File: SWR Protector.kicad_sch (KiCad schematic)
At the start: 29 parts, among them J1 Barrel_Jack, J2 Barrel_Jack, J3 transceiver, J4 antenna, K2 ATX209, Q1 2N3904, T1 1:12, T2 1:12, U1 LM78L05_TO92, U2 LM358

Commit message: updated BNC to something reasonable, w/ Ron\'s help
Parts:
- J3, J4: footprint Connector_Coaxial:BNC_TEConnectivity_1478035_Horizontal -> Connector_Coaxial:BNC_Amphenol_B6252HB-NPP3G-50_Horizontal
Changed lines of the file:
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@@
   (title_block
     (title "SWR Protector WA7GIL")
-    (date "2023-05-09")
-    (rev "0.6")
+    (date "2023-05-10")
+    (rev "0.7")
   )
   (junction (at 181.61 138.43) (diameter 0) (color 0 0 0 0)
@@
       (effects (font (size 1.27 1.27)) (justify left))
     )
-    (property "Footprint" "Connector_Coaxial:BNC_TEConnectivity_1478035_Horizontal" (at 134.62 35.56 0)
+    (property "Footprint" "Connector_Coaxial:BNC_Amphenol_B6252HB-NPP3G-50_Horizontal" (at 134.62 35.56 0)
       (effects (font (size 1.27 1.27)) hide)
     )
@@
       (effects (font (size 1.27 1.27)) (justify left))
     )
-    (property "Footprint" "Connector_Coaxial:BNC_TEConnectivity_1478035_Horizontal" (at 48.26 35.56 0)
-      (effects (font (size 1.27 1.27)) hide)
-    )
+    (property "Footprint" "Connector_Coaxial:BNC_Amphenol_B6252HB-NPP3G-50_Horizontal" (at 48.26 35.56 0)
+      (effects (font (size 1.27 1.27)) hide)
+    )

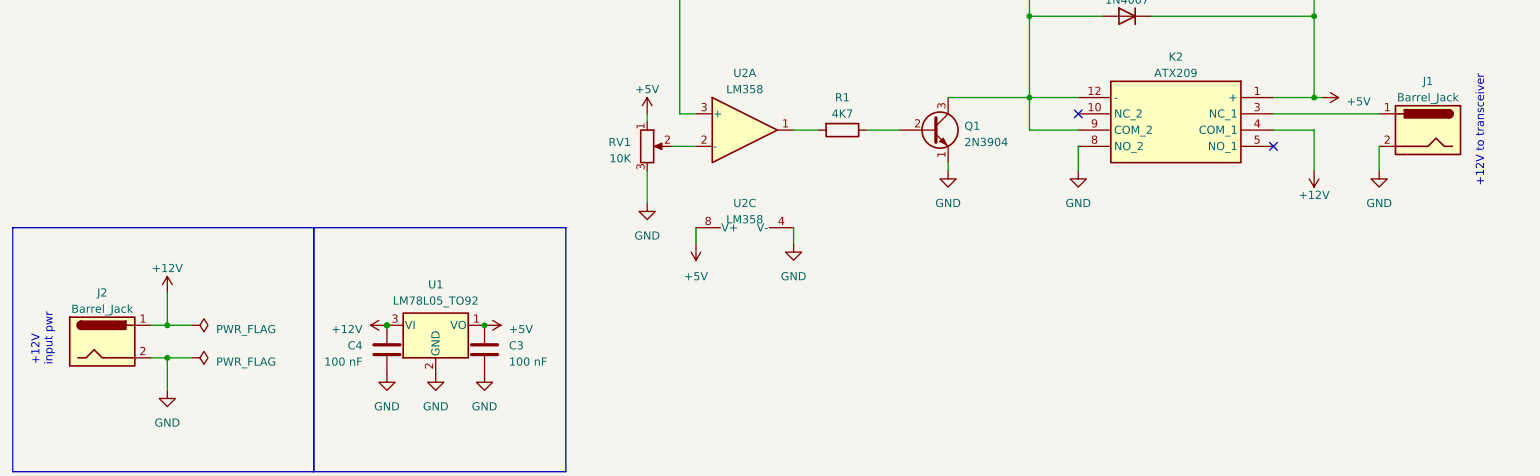
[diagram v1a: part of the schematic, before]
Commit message: changed footprint for BNC, barrel connectors to make them normal
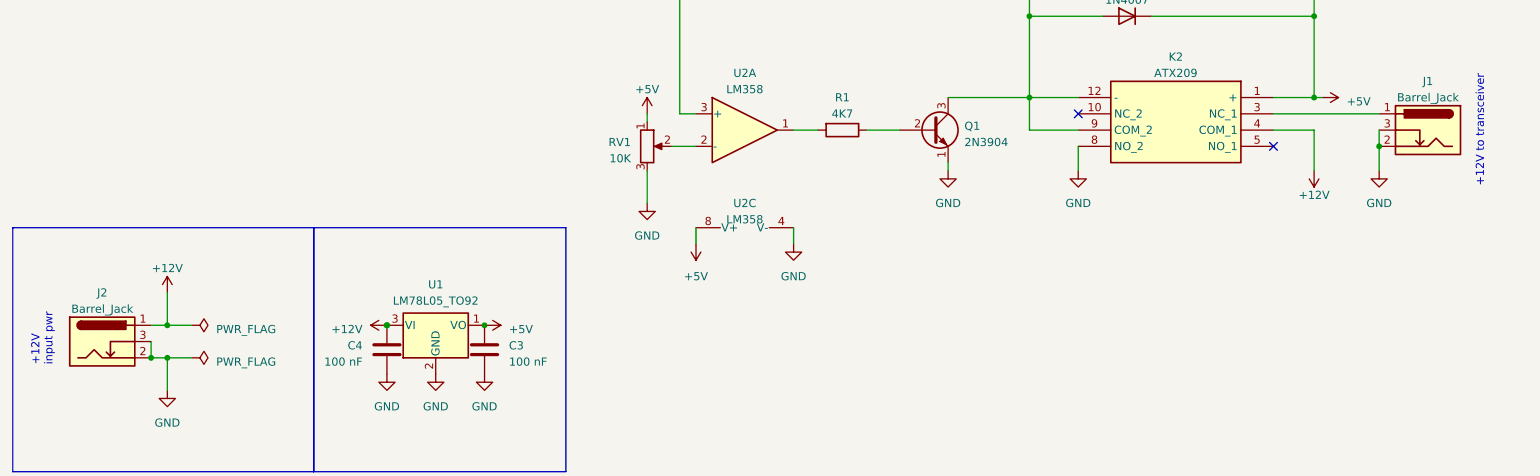
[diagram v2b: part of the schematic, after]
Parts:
- removed J1, J2: Barrel_Jack, Connector_BarrelJack:BarrelJack_CUI_PJ-063AH_Horizontal, symbol Connector:Barrel_Jack
- added J1, J2: Barrel_Jack, Connector_BarrelJack:BarrelJack_Horizontal, symbol Connector:Barrel_Jack_Switch
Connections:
- net +12V: now also J2.1
- net GND: now also J1.2, J1.3, J2.2, J2.3
- net at K2.3 (NC_1): now also J1.1
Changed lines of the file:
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@@
     (rev "0.7")
   )
+  (junction (at 44.45 179.07) (diameter 0) (color 0 0 0 0)
+  )
   (junction (at 181.61 138.43) (diameter 0) (color 0 0 0 0)
   )
@@
   )
   (junction (at 134.62 80.01) (diameter 0) (color 0 0 0 0)
+  )
+  (junction (at 236.22 146.05) (diameter 0) (color 0 0 0 0)
   )
   (junction (at 134.62 60.96) (diameter 0) (color 0 0 0 0)
@@
     (stroke (width 0) (type default))
   )
+  (wire (pts (xy 44.45 176.53) (xy 44.45 179.07))
+    (stroke (width 0) (type default))
+  )
   (wire (pts (xy 181.61 114.3) (xy 181.61 125.73))
     (stroke (width 0) (type default))
@@
   )
   (wire (pts (xy 49.53 80.01) (xy 50.8 80.01))
+    (stroke (width 0) (type default))
+  )
+  (wire (pts (xy 236.22 143.51) (xy 236.22 146.05))
     (stroke (width 0) (type default))
   )
@@
         (path "/46027dd5-036f-43c6-98e1-c4cfe473ecd7"
           (reference "D1") (unit 1)
-        )
-      )
-    )
-  )
-  (symbol (lib_id "Connector:Barrel_Jack") (at 36.83 176.53 0) (unit 1)
-    (in_bom yes) (on_board yes) (dnp no)
-    (property "Reference" "J2" (at 36.83 168.91 0)
-      (effects (font (size 1.27 1.27)))
-    )
-    (property "Value" "Barrel_Jack" (at 36.83 171.45 0)
-      (effects (font (size 1.27 1.27)))
-    )
-    (property "Footprint" "Connector_BarrelJack:BarrelJack_CUI_PJ-063AH_Horizontal" (at 38.1 177.546 0)
-      (effects (font (size 1.27 1.27)) hide)
-    )
-    (property "Datasheet" "~" (at 38.1 177.546 0)
-      (effects (font (size 1.27 1.27)) hide)
-    )
-    (pin "1")
-    (pin "2")
-    (instances
-      (project "SWR Protector"
-        (path "/46027dd5-036f-43c6-98e1-c4cfe473ecd7"
-          (reference "J2") (unit 1)
         )
       )
@@
     )
   )
+  (symbol (lib_id "Connector:Barrel_Jack_Switch") (at 243.84 143.51 0) (mirror y) (unit 1)
+    (in_bom yes) (on_board yes) (dnp no)
+    (property "Reference" "J1" (at 243.84 135.89 0)
+      (effects (font (size 1.27 1.27)))
+    )
+    (property "Value" "Barrel_Jack" (at 243.84 138.43 0)
+      (effects (font (size 1.27 1.27)))
+    )
+    (property "Footprint" "Connector_BarrelJack:BarrelJack_Horizontal" (at 242.57 144.526 0)
+      (effects (font (size 1.27 1.27)) hide)
+    )
+    (property "Datasheet" "~" (at 242.57 144.526 0)
+      (effects (font (size 1.27 1.27)) hide)
+    )
+    (pin "1")
+    (pin "2")
+    (pin "3")
+    (instances
+      (project "SWR Protector"
+        (path "/46027dd5-036f-43c6-98e1-c4cfe473ecd7"
+          (reference "J1") (unit 1)
+        )
+      )
+    )
+  )
   (symbol (lib_id "Device:R") (at 142.24 60.96 90) (unit 1)
     (in_bom yes) (on_board yes) (dnp no)
@@
     )
   )
+  (symbol (lib_id "Connector:Barrel_Jack_Switch") (at 36.83 176.53 0) (unit 1)
+    (in_bom yes) (on_board yes) (dnp no) (fields_autoplaced)
+    (property "Reference" "J2" (at 36.83 168.91 0)
+      (effects (font (size 1.27 1.27)))
+    )
+    (property "Value" "Barrel_Jack" (at 36.83 171.45 0)
+      (effects (font (size 1.27 1.27)))
+    )
+    (property "Footprint" "Connector_BarrelJack:BarrelJack_Horizontal" (at 38.1 177.546 0)
+      (effects (font (size 1.27 1.27)) hide)
+    )
+    (property "Datasheet" "~" (at 38.1 177.546 0)
+      (effects (font (size 1.27 1.27)) hide)
+    )
+    (pin "1")
+    (pin "2")
+    (pin "3")
+    (instances
+      (project "SWR Protector"
+        (path "/46027dd5-036f-43c6-98e1-c4cfe473ecd7"
+          (reference "J2") (unit 1)
+        )
+      )
+    )
+  )
   (symbol (lib_id "power:GND") (at 123.19 80.01 270) (unit 1)
     (in_bom yes) (on_board yes) (dnp no) (fields_autoplaced)
@@
         )
       )
-    )
-  )
-  (symbol (lib_id "Connector:Barrel_Jack") (at 243.84 143.51 0) (mirror y) (unit 1)
-    (in_bom yes) (on_board yes) (dnp no)
-    (property "Reference" "J1" (at 243.84 135.89 0)
-      (effects (font (size 1.27 1.27)))
-    )
-    (property "Value" "Barrel_Jack" (at 243.84 138.43 0)
-      (effects (font (size 1.27 1.27)))
-    )
-    (property "Footprint" "Connector_BarrelJack:BarrelJack_CUI_PJ-063AH_Horizontal" (at 242.57 144.526 0)
-      (effects (font (size 1.27 1.27)) hide)
-    )
-    (property "Datasheet" "~" (at 242.57 144.526 0)
-      (effects (font (size 1.27 1.27)) hide)
-    )
-    (pin "1")
-    (pin "2")
-    (instances
-      (project "SWR Protector"
-        (path "/46027dd5-036f-43c6-98e1-c4cfe473ecd7"
-          (reference "J1") (unit 1)
-        )
-      )

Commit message: added mounting holes; checkpoint progress on footprints for connectors
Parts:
- RV1: footprint Potentiometer_THT:Potentiometer_Alpha_RD901F-40-00D_Single_Vertical -> Potentiometer_THT:Potentiometer_Bourns_3266Y_Vertical
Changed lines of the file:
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@@
       (effects (font (size 1.27 1.27)) (justify right))
     )
-    (property "Footprint" "Potentiometer_THT:Potentiometer_Alpha_RD901F-40-00D_Single_Vertical" (at 121.92 146.05 0)
+    (property "Footprint" "Potentiometer_THT:Potentiometer_Bourns_3266Y_Vertical" (at 121.92 146.05 0)
       (effects (font (size 1.27 1.27)) hide)
     )
